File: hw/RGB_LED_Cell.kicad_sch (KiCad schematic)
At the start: 4 parts

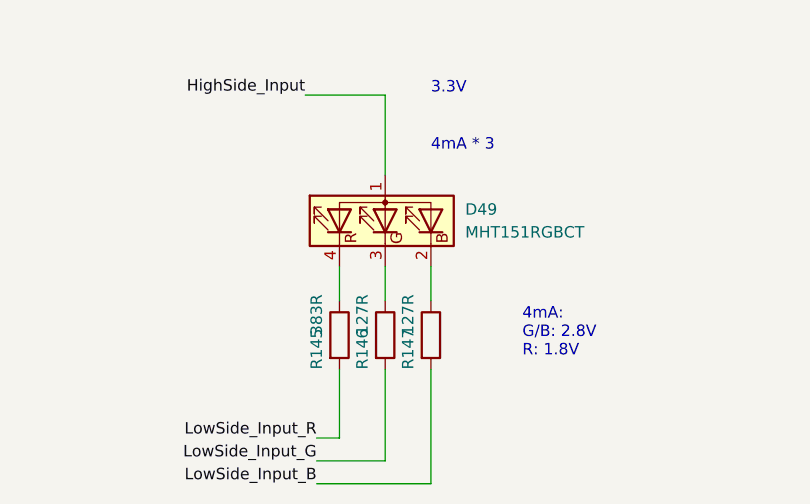
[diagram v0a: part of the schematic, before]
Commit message: updated and fix ERCs
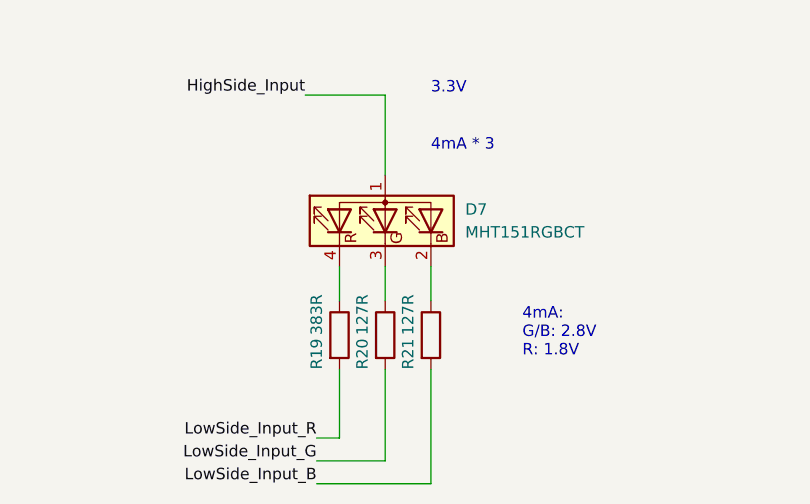
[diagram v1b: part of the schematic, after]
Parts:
- renumbered D49 to D7, R145 to R19, R146 to R20, R147 to R21

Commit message: routing
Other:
- moved on the sheet: R19, R20, R21

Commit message: updated netclasses
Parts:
- renumbered D7 to D49, R19 to R145, R20 to R146, R21 to R147
